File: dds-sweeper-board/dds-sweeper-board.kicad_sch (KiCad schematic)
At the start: 12 parts, among them J1 REF CLK OUT, J3 1V8, J4 AD9959 Eval Header, J5 Trigger In, J6 RESET, J7 DDS PWR, U1 Pico, U3 XC6210B18

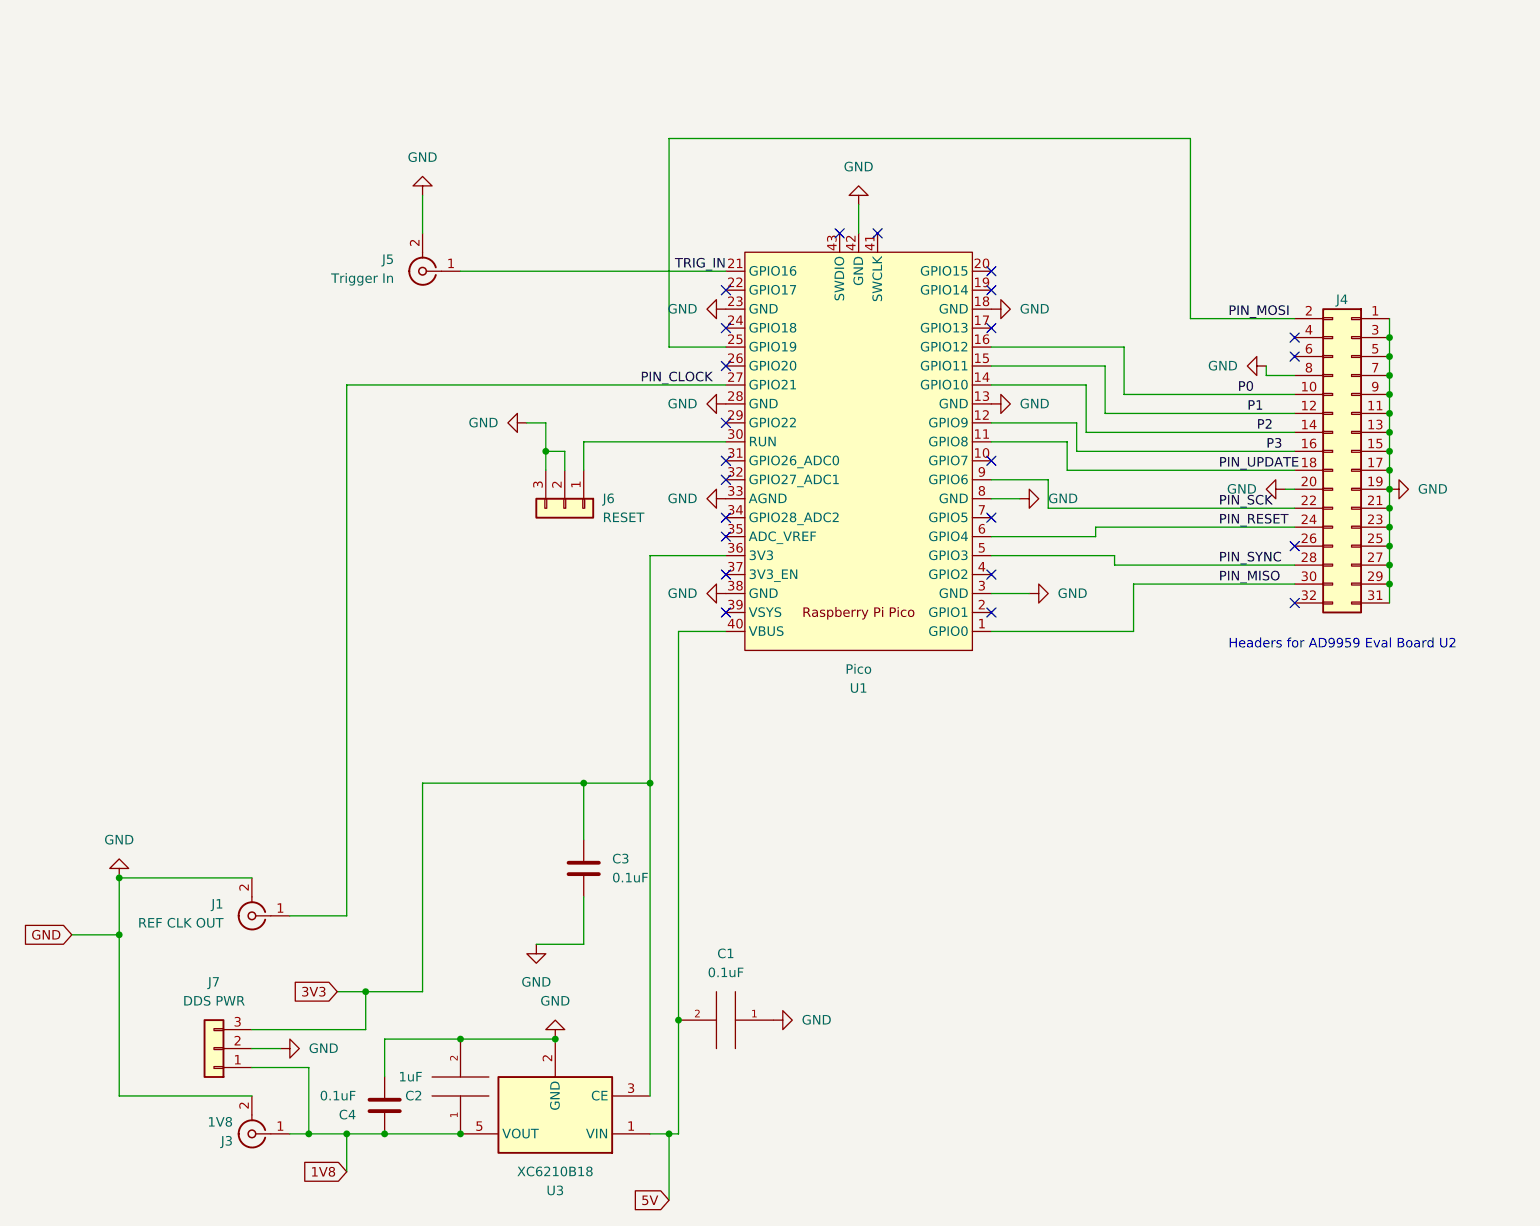
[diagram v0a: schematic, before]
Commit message: Update breakout board to have an input buffer on the trigger line.
Should help with longer cable runs on the trigger input.
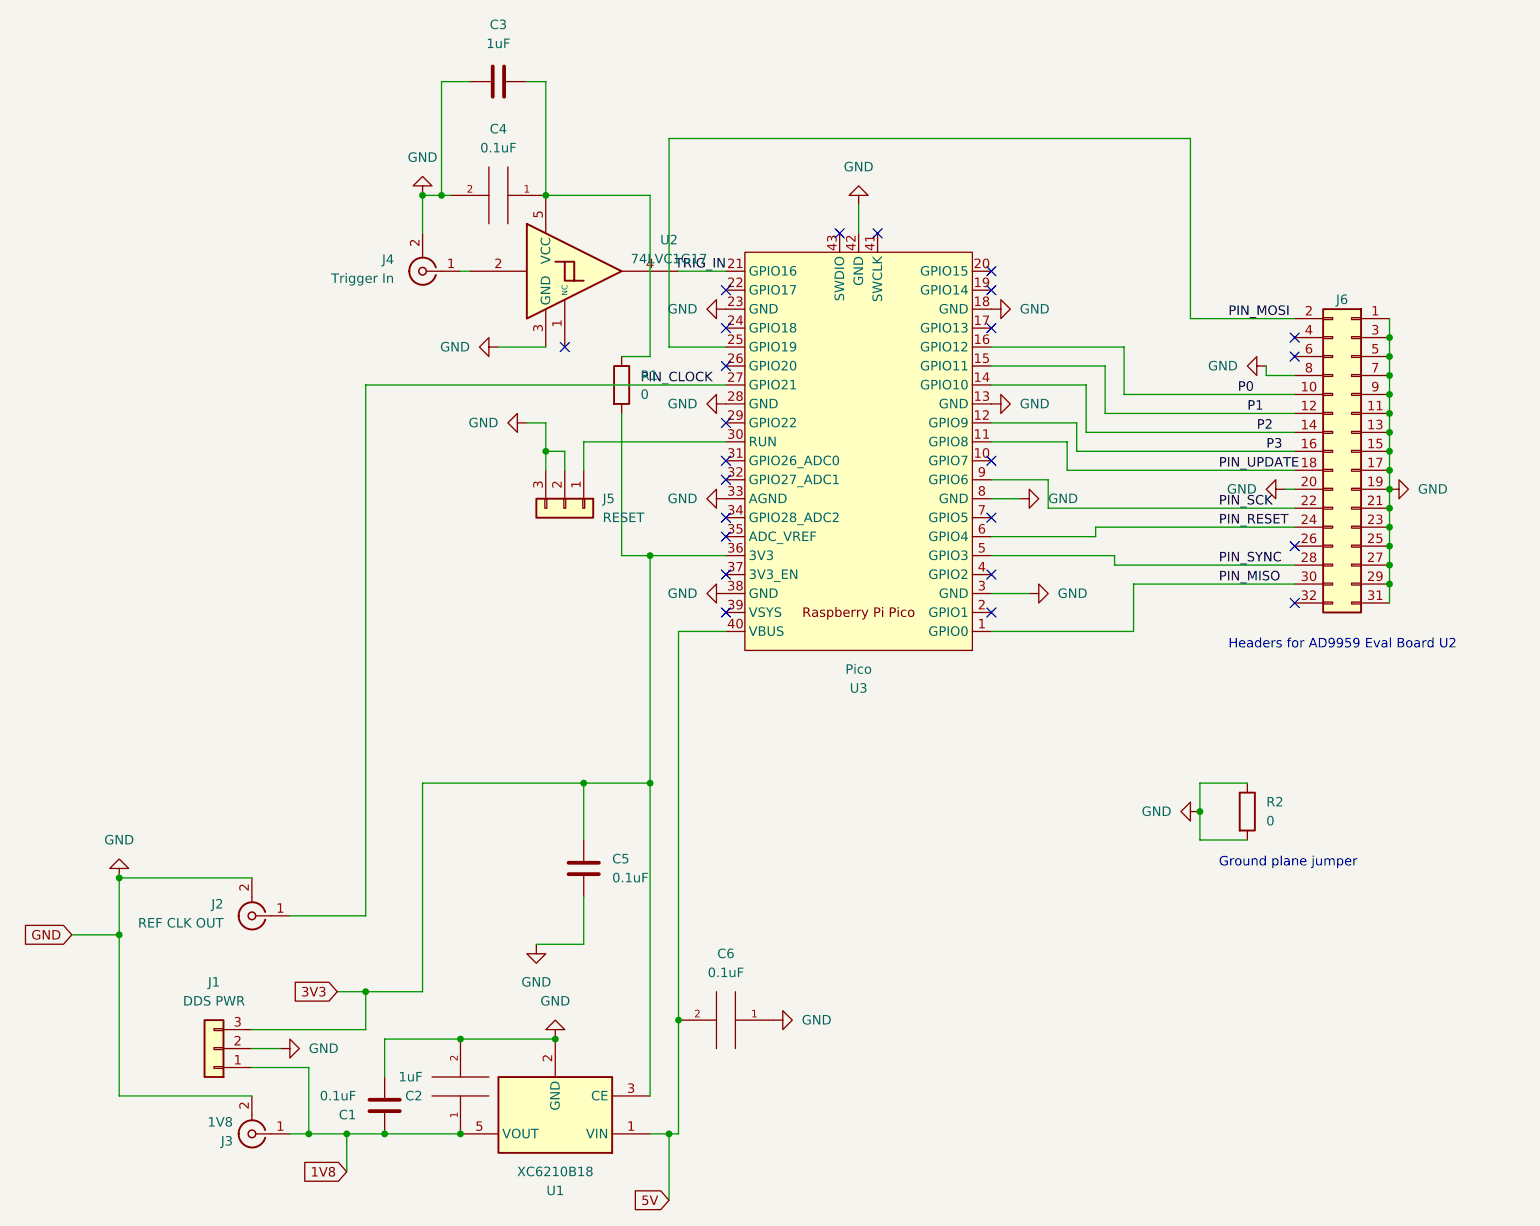
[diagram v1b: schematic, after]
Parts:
- added C3: 1uF, Capacitor_SMD:C_0805_2012Metric_Pad1.18x1.45mm_HandSolder, symbol Device:C
- added C4: 0.1uF, Capacitor_SMD:C_0805_2012Metric_Pad1.18x1.45mm_HandSolder, symbol pspice:CAP
- added R1, R2: 0, Resistor_SMD:R_1206_3216Metric_Pad1.30x1.75mm_HandSolder, symbol Device:R
- added U2: 74LVC1G17, Package_TO_SOT_SMD:SOT-23-5, symbol 74xGxx:74LVC1G17
- renumbered C4 to C1, C3 to C5, C1 to C6, J7 to J1, J1 to J2, J5 to J4, J6 to J5, J4 to J6, U3 to U1, U1 to U3
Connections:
- net 3V3: now also R1.2
- net GND: now also C3.2, C4.2, R2.1, R2.2, U2.3 (GND)
- net TRIG_IN: now also U2.4; no longer J4.1 (In)
- new net: C3.1, C4.1, R1.1, U2.5 (VCC)
- new net: J4.1 (In), U2.2
- no-connect marks 23 -> 24
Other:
- note added: "Ground plane jumper"

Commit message: Update KiCAD project with proper header footprint (instead of sockets) and add 3D components so 3D board render is correct.
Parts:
- J1, J5: footprint Connector_PinSocket_2.54mm:PinSocket_1x03_P2.54mm_Vertical -> Connector_PinHeader_2.54mm:PinHeader_1x03_P2.54mm_Vertical
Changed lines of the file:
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@@
     (pin "1")
     (instances
-      (project "dds-sweeper-board-buffers"
+      (project "dds-sweeper-board"
         (path "/2fc70846-1f68-48b7-a1be-f7617c334c44"
           (reference "#PWR09") (unit 1)
@@
     (pin "2")
     (instances
-      (project "dds-sweeper-board-buffers"
+      (project "dds-sweeper-board"
         (path "/2fc70846-1f68-48b7-a1be-f7617c334c44"
           (reference "C4") (unit 1)
@@
     (pin "2")
     (instances
-      (project "dds-sweeper-board-buffers"
+      (project "dds-sweeper-board"
         (path "/2fc70846-1f68-48b7-a1be-f7617c334c44"
           (reference "C2") (unit 1)
@@
     (pin "9")
     (instances
-      (project "dds-sweeper-board-buffers"
+      (project "dds-sweeper-board"
         (path "/2fc70846-1f68-48b7-a1be-f7617c334c44"
           (reference "U3") (unit 1)
@@
     (pin "2")
     (instances
-      (project "dds-sweeper-board-buffers"
+      (project "dds-sweeper-board"
         (path "/2fc70846-1f68-48b7-a1be-f7617c334c44"
           (reference "R2") (unit 1)
@@
     (pin "1")
     (instances
-      (project "dds-sweeper-board-buffers"
+      (project "dds-sweeper-board"
         (path "/2fc70846-1f68-48b7-a1be-f7617c334c44"
           (reference "#PWR019") (unit 1)
@@
     (pin "1")
     (instances
-      (project "dds-sweeper-board-buffers"
+      (project "dds-sweeper-board"
         (path "/2fc70846-1f68-48b7-a1be-f7617c334c44"
           (reference "#PWR015") (unit 1)
@@
     (pin "2")
     (instances
-      (project "dds-sweeper-board-buffers"
+      (project "dds-sweeper-board"
         (path "/2fc70846-1f68-48b7-a1be-f7617c334c44"
           (reference "J2") (unit 1)
@@
     (pin "2")
     (instances
-      (project "dds-sweeper-board-buffers"
+      (project "dds-sweeper-board"
         (path "/2fc70846-1f68-48b7-a1be-f7617c334c44"
           (reference "R1") (unit 1)
@@
     (pin "1")
     (instances
-      (project "dds-sweeper-board-buffers"
+      (project "dds-sweeper-board"
         (path "/2fc70846-1f68-48b7-a1be-f7617c334c44"
           (reference "#PWR010") (unit 1)
@@
     (pin "1")
     (instances
-      (project "dds-sweeper-board-buffers"
+      (project "dds-sweeper-board"
         (path "/2fc70846-1f68-48b7-a1be-f7617c334c44"
           (reference "#PWR021") (unit 1)
@@
     (pin "1")
     (instances
-      (project "dds-sweeper-board-buffers"
+      (project "dds-sweeper-board"
         (path "/2fc70846-1f68-48b7-a1be-f7617c334c44"
           (reference "#PWR06") (unit 1)
@@
     (pin "2")
     (instances
-      (project "dds-sweeper-board-buffers"
+      (project "dds-sweeper-board"
         (path "/2fc70846-1f68-48b7-a1be-f7617c334c44"
           (reference "J3") (unit 1)
@@
     (pin "1")
     (instances
-      (project "dds-sweeper-board-buffers"
+      (project "dds-sweeper-board"
         (path "/2fc70846-1f68-48b7-a1be-f7617c334c44"
           (reference "#PWR05") (unit 1)
@@
     (pin "1")
     (instances
-      (project "dds-sweeper-board-buffers"
+      (project "dds-sweeper-board"
         (path "/2fc70846-1f68-48b7-a1be-f7617c334c44"
           (reference "#PWR018") (unit 1)
@@
       (effects (font (size 1.27 1.27)))
     )
-    (property "Footprint" "Connector_PinSocket_2.54mm:PinSocket_1x03_P2.54mm_Vertical" (at 38.1 181.61 0)
+    (property "Footprint" "Connector_PinHeader_2.54mm:PinHeader_1x03_P2.54mm_Vertical" (at 38.1 181.61 0)
       (effects (font (size 1.27 1.27)) hide)
     )
@@
     (pin "1")
     (instances
-      (project "dds-sweeper-board-buffers"
+      (project "dds-sweeper-board"
         (path "/2fc70846-1f68-48b7-a1be-f7617c334c44"
           (reference "J1") (unit 1)
@@
     (pin "1")
     (instances
-      (project "dds-sweeper-board-buffers"
+      (project "dds-sweeper-board"
         (path "/2fc70846-1f68-48b7-a1be-f7617c334c44"
           (reference "#PWR020") (unit 1)
@@
     (pin "1")
     (instances
-      (project "dds-sweeper-board-buffers"
+      (project "dds-sweeper-board"
         (path "/2fc70846-1f68-48b7-a1be-f7617c334c44"
           (reference "#PWR07") (unit 1)
@@
     (pin "1")
     (instances
-      (project "dds-sweeper-board-buffers"
+      (project "dds-sweeper-board"
         (path "/2fc70846-1f68-48b7-a1be-f7617c334c44"
           (reference "#PWR017") (unit 1)
@@
     (pin "1")
     (instances
-      (project "dds-sweeper-board-buffers"
+      (project "dds-sweeper-board"
         (path "/2fc70846-1f68-48b7-a1be-f7617c334c44"
           (reference "#PWR02") (unit 1)
@@
     (pin "1")
     (instances
-      (project "dds-sweeper-board-buffers"
+      (project "dds-sweeper-board"
         (path "/2fc70846-1f68-48b7-a1be-f7617c334c44"
           (reference "#PWR014") (unit 1)
@@
     (pin "2")
     (instances
-      (project "dds-sweeper-board-buffers"
+      (project "dds-sweeper-board"
         (path "/2fc70846-1f68-48b7-a1be-f7617c334c44"
           (reference "C3") (unit 1)
@@
     (pin "1")
     (instances
-      (project "dds-sweeper-board-buffers"
+      (project "dds-sweeper-board"
         (path "/2fc70846-1f68-48b7-a1be-f7617c334c44"
           (reference "#PWR013") (unit 1)
@@
     (pin "1")
     (instances
-      (project "dds-sweeper-board-buffers"
+      (project "dds-sweeper-board"
         (path "/2fc70846-1f68-48b7-a1be-f7617c334c44"
           (reference "#PWR012") (unit 1)
@@
       (effects (font (size 1.27 1.27)) (justify left))
     )
-    (property "Footprint" "Connector_PinSocket_2.54mm:PinSocket_1x03_P2.54mm_Vertical" (at 85.09 109.22 0)
+    (property "Footprint" "Connector_PinHeader_2.54mm:PinHeader_1x03_P2.54mm_Vertical" (at 85.09 109.22 0)
       (effects (font (size 1.27 1.27)) hide)
     )
@@
     (pin "1")
     (instances
-      (project "dds-sweeper-board-buffers"
+      (project "dds-sweeper-board"
         (path "/2fc70846-1f68-48b7-a1be-f7617c334c44"
           (reference "J5") (unit 1)
@@
     (pin "30")
     (instances
-      (project "dds-sweeper-board-buffers"
+      (project "dds-sweeper-board"
         (path "/2fc70846-1f68-48b7-a1be-f7617c334c44"
           (reference "J6") (unit 1)
@@
     (pin "2")
     (instances
-      (project "dds-sweeper-board-buffers"
+      (project "dds-sweeper-board"
         (path "/2fc70846-1f68-48b7-a1be-f7617c334c44"
           (reference "J4") (unit 1)
@@
     (pin "2")
     (instances
-      (project "dds-sweeper-board-buffers"
+      (project "dds-sweeper-board"
         (path "/2fc70846-1f68-48b7-a1be-f7617c334c44"
           (reference "C1") (unit 1)
@@
     (pin "1")
     (instances
-      (project "dds-sweeper-board-buffers"
+      (project "dds-sweeper-board"
         (path "/2fc70846-1f68-48b7-a1be-f7617c334c44"
           (reference "#PWR011") (unit 1)
@@
     (pin "2")
     (instances
-      (project "dds-sweeper-board-buffers"
+      (project "dds-sweeper-board"
         (path "/2fc70846-1f68-48b7-a1be-f7617c334c44"
           (reference "C5") (unit 1)
@@
     (pin "1")
     (instances
-      (project "dds-sweeper-board-buffers"
+      (project "dds-sweeper-board"
         (path "/2fc70846-1f68-48b7-a1be-f7617c334c44"
           (reference "U2") (unit 1)
@@
     (pin "1")
     (instances
-      (project "dds-sweeper-board-buffers"
+      (project "dds-sweeper-board"
         (path "/2fc70846-1f68-48b7-a1be-f7617c334c44"
           (reference "#PWR01") (unit 1)
@@
     (pin "1")
     (instances
-      (project "dds-sweeper-board-buffers"
+      (project "dds-sweeper-board"
         (path "/2fc70846-1f68-48b7-a1be-f7617c334c44"
           (reference "#PWR04") (unit 1)
@@
     (pin "1")
     (instances
-      (project "dds-sweeper-board-buffers"
+      (project "dds-sweeper-board"
         (path "/2fc70846-1f68-48b7-a1be-f7617c334c44"
           (reference "#PWR016") (unit 1)
@@
     (pin "5")
     (instances
-      (project "dds-sweeper-board-buffers"
+      (project "dds-sweeper-board"
         (path "/2fc70846-1f68-48b7-a1be-f7617c334c44"
           (reference "U1") (unit 1)
@@
     (pin "1")
     (instances
-      (project "dds-sweeper-board-buffers"
+      (project "dds-sweeper-board"
         (path "/2fc70846-1f68-48b7-a1be-f7617c334c44"
           (reference "#PWR08") (unit 1)
@@
     (pin "1")
     (instances
-      (project "dds-sweeper-board-buffers"
+      (project "dds-sweeper-board"
         (path "/2fc70846-1f68-48b7-a1be-f7617c334c44"
           (reference "#PWR03") (unit 1)
@@
     (pin "2")
     (instances
-      (project "dds-sweeper-board-buffers"
+      (project "dds-sweeper-board"
         (path "/2fc70846-1f68-48b7-a1be-f7617c334c44"
           (reference "C6") (unit 1)
